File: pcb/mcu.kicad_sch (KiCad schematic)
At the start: 18 parts, among them J1 AVR-UPDI-6, U1 ATtiny1616-MNR

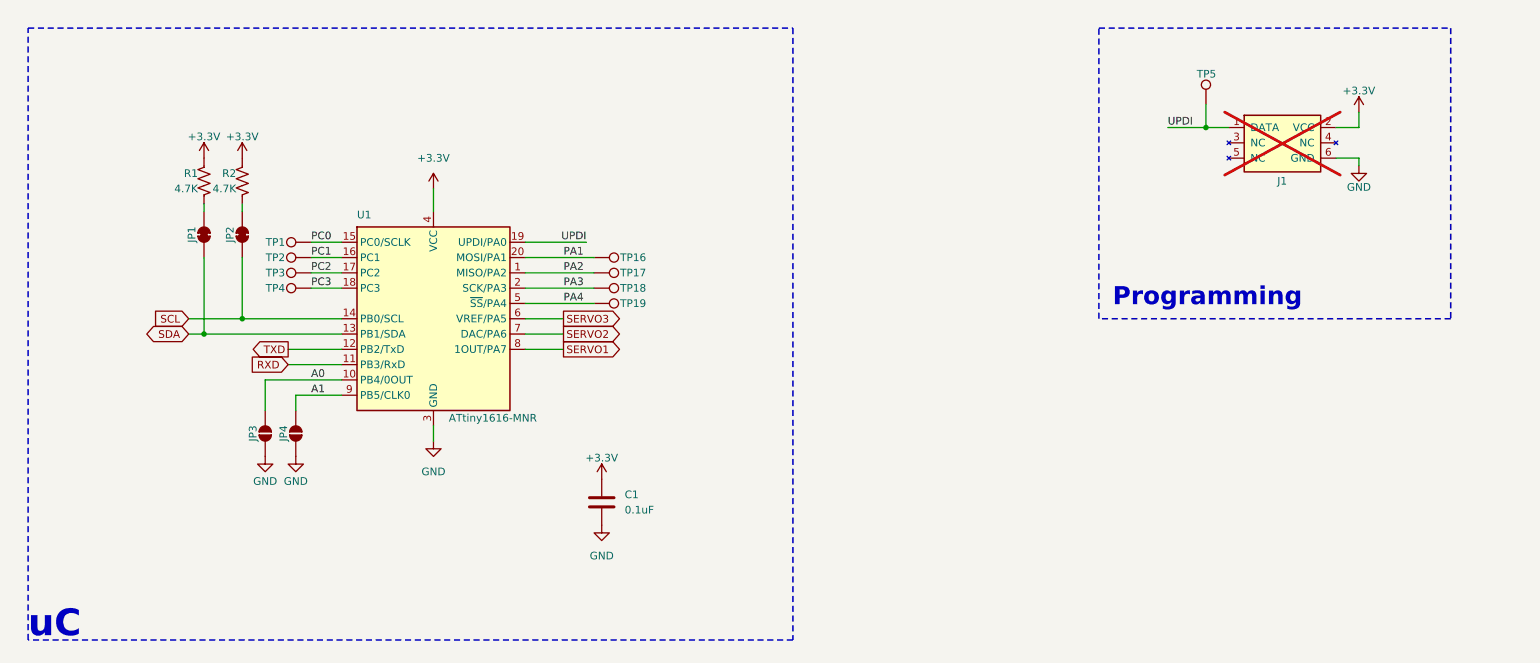
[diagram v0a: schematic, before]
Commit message: Added status leds
forced to reroute entire board
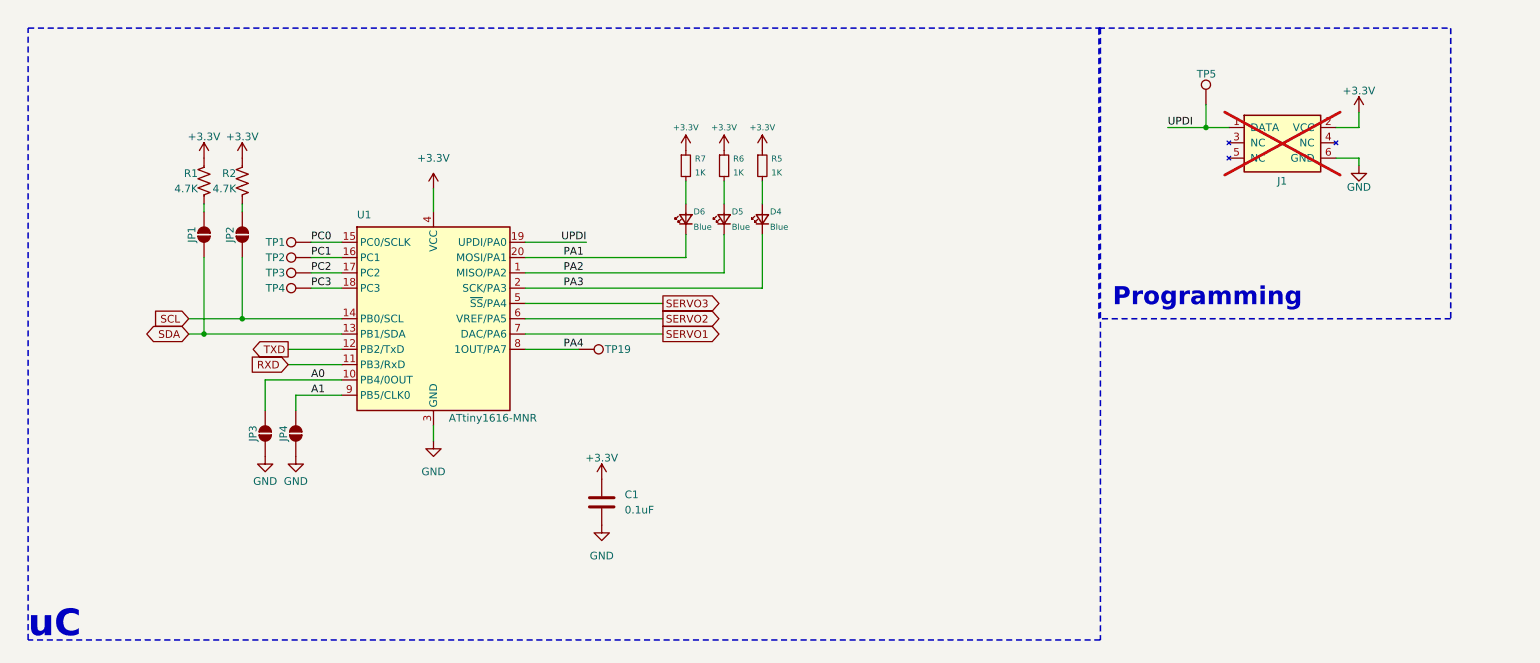
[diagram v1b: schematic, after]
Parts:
- removed TP16, TP17, TP18: ~, CRGM Mechanical:TestPoint_Pad_D1.0mm, symbol Connector:TestPoint
- added D4, D5, D6: Blue, CRGM Passive:LED_0603_1608Metric, symbol Device:LED_Small
- added R5, R6, R7: 1K, CRGM Passive:R_0603_1608Metric, symbol Device:R_Small
- JP1, JP2: footprint CRGM Connector:SolderJumper-2_P1.3mm_Bridged_RoundedPad1.0x1.5mm -> CRGM Connector:SolderJumper-2_P1.3mm_Open_RoundedPad1.0x1.5mm; symbol Jumper:SolderJumper_2_Bridged -> CRGM Connector:SolderJumper_2_Open
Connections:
- net +3.3V: now also R5.1, R6.1, R7.1
- net PA1: now also D6.1 (K)
- net PA2: now also D5.1 (K)
- net PA3: now also D4.1 (K)
- net PA4: now also U1.8 (1OUT/PA7); no longer U1.5 (~{SS}/PA4)
- net SERVO1: now also U1.7 (DAC/PA6); no longer U1.8 (1OUT/PA7)
- net SERVO2: now also U1.6 (VREF/PA5); no longer U1.7 (DAC/PA6)
- net SERVO3: now also U1.5 (~{SS}/PA4); no longer U1.6 (VREF/PA5)
- new net: D5.2 (A), R6.2
- new net: D6.2 (A), R7.2
- new net: D4.2 (A), R5.2
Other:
- moved on the sheet: TP19

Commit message: Added servo power and filtering
Added connection for servo power
Added solder jumper for servo power to 5V
Added caps to servo power
Added bulk decoupling caps
Added TVS to various inputs
Updated renders
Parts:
- removed C1: 0.1uF, CRGM Passive:C_0603_1608Metric, symbol Device:C
- added C1: 0.1uF, CRGM Passive:C_0603_1608Metric, symbol Device:C_Small
- renumbered D6 to D1, D5 to D2, D4 to D3, R7 to R3, R6 to R4, TP19 to TP5, TP5 to TP6
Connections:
- net +3.3V: now also C1.1
- net GND: now also C1.2

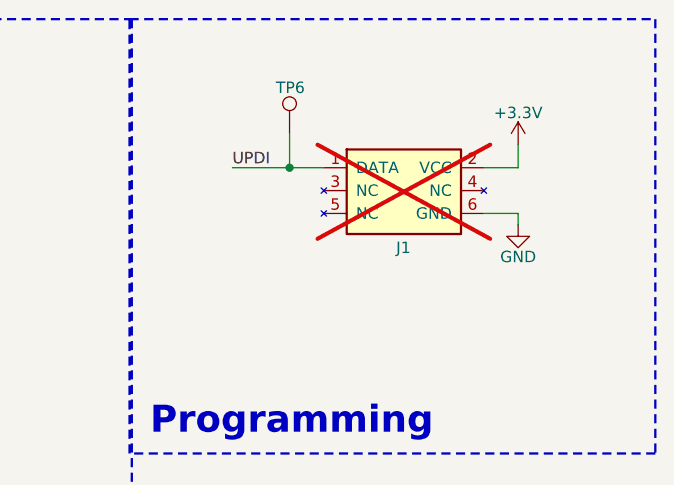
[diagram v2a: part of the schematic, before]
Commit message: Adjusting back on lessons learned from 1.1,
Added skilkscreen
Moved UART to UPDI connector
Created room for 4th servo connector?
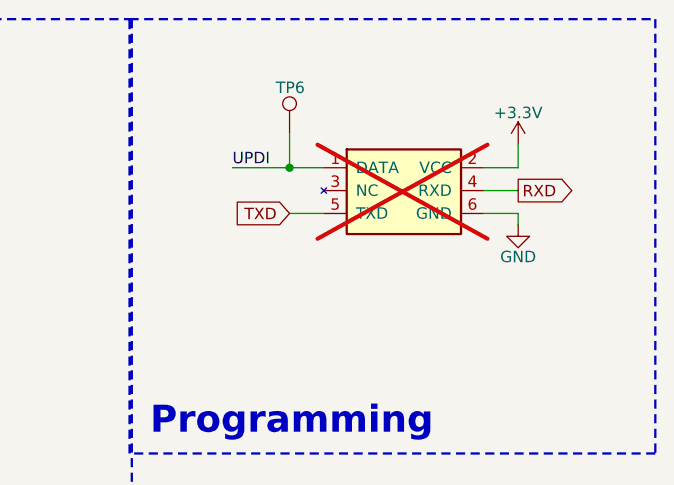
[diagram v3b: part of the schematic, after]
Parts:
- J1: symbol CRGM Connector:AVR-UPDI-6 -> CRGM Connector:AVR-UPDI-UART-6; now in the parts list
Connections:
- net RXD: now also J1.4 (RXD)
- net TXD: now also J1.5 (TXD)
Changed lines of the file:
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@@
+	(wire
+		(pts
+			(xy 246.38 44.45) (xy 242.57 44.45)
+		)
+		(stroke
+			(width 0)
+			(type default)
+		)
+	)
 	(wire
 		(pts
@@
 		(pts
 			(xy 107.95 78.74) (xy 116.84 78.74)
+		)
+		(stroke
+			(width 0)
+			(type default)
+		)
+	)
+	(wire
+		(pts
+			(xy 220.98 46.99) (xy 224.79 46.99)
 		)
 		(stroke
@@
 		(property "Intersheetrefs" "${INTERSHEET_REFS}"
 			(at 44.4054 76.2 0)
+			(effects
+				(font
+					(size 1.27 1.27)
+				)
+				(justify right)
+			)
+		)
+	)
+	(global_label "RXD"
+		(shape output)
+		(at 246.38 44.45 0)
+		(fields_autoplaced yes)
+		(effects
+			(font
+				(size 1.27 1.27)
+			)
+			(justify left)
+		)
+		(property "Intersheetrefs" "${INTERSHEET_REFS}"
+			(at 253.1147 44.45 0)
+			(effects
+				(font
+					(size 1.27 1.27)
+				)
+				(justify left)
+			)
+		)
+	)
+	(global_label "TXD"
+		(shape input)
+		(at 220.98 46.99 180)
+		(fields_autoplaced yes)
+		(effects
+			(font
+				(size 1.27 1.27)
+			)
+			(justify right)
+		)
+		(property "Intersheetrefs" "${INTERSHEET_REFS}"
+			(at 214.5477 46.99 0)
 			(effects
 				(font
@@
 	)
 	(symbol
-		(lib_id "CRGM Connector:AVR-UPDI-6")
+		(lib_id "CRGM Connector:AVR-UPDI-UART-6")
 		(at 233.68 45.72 0)
 		(unit 1)
 		(exclude_from_sim no)
-		(in_bom no)
+		(in_bom yes)
 		(on_board yes)
 		(dnp yes)
@@
 				)
 				(justify right)
+				(hide yes)
 			)
 		)
@@
 		)
 		(property "Footprint" "CRGM Connector:PinHeader_2x03_P2.54mm_Vertical_SMD"
-			(at 227.33 46.99 90)
+			(at 233.68 58.674 0)
 			(effects
 				(font
@@
 			)
 		)
-		(property "Description" "Atmel 6-pin UPDI connector"
+		(property "Description" "Atmel 6-pin UPDI + UART connector"
 			(at 233.68 56.388 0)
 			(effects

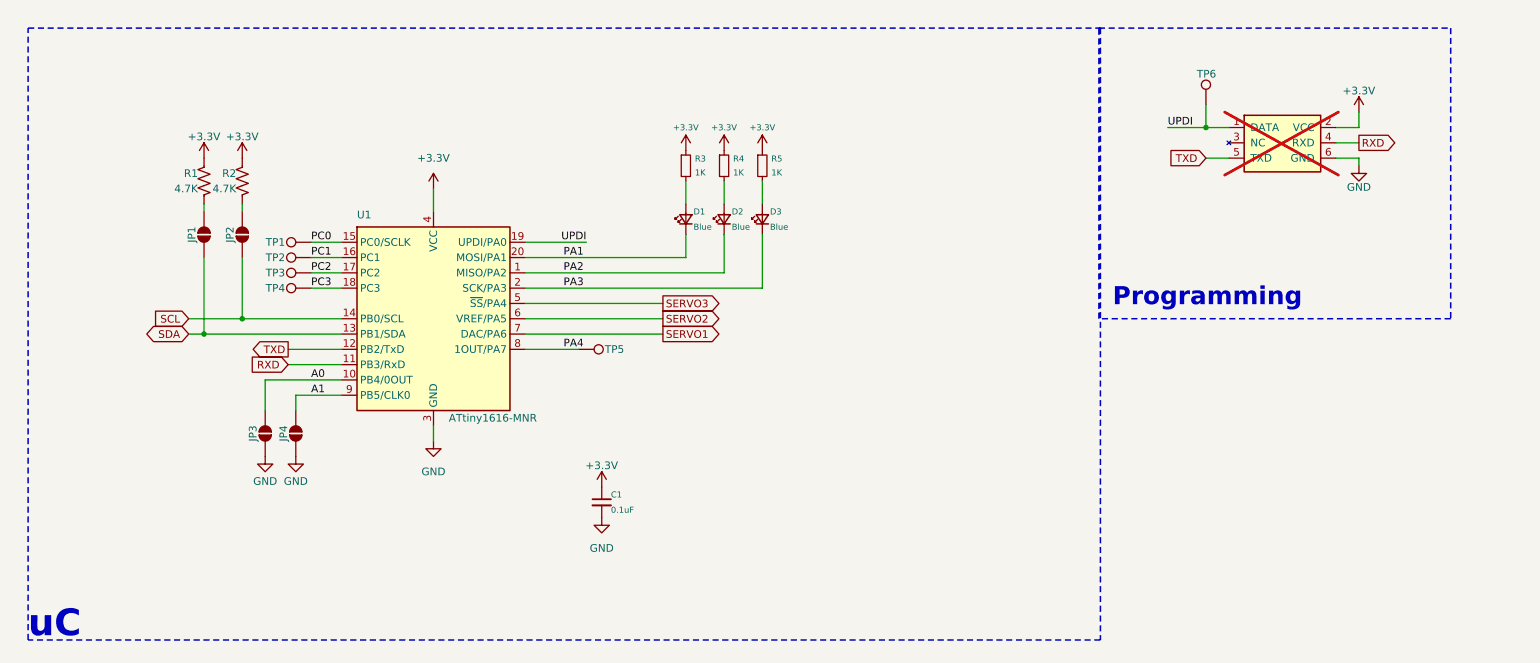
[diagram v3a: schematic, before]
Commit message: changed connectors to vertical
Updated connectors with ground on mounting points
Updated and rerouted
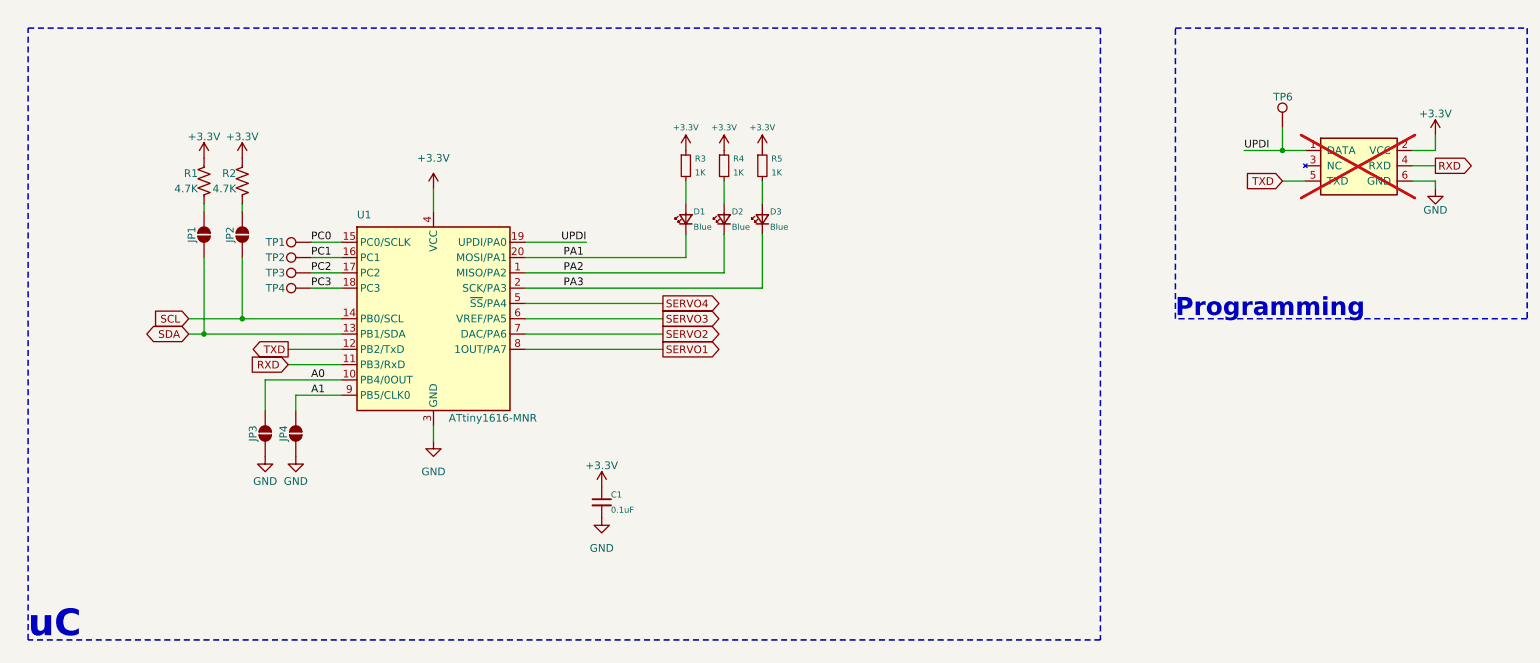
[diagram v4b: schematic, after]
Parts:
- removed TP5: ~, CRGM Mechanical:TestPoint_Pad_D1.0mm, symbol Connector:TestPoint
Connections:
- net PA4 is gone; now on net SERVO1: U1.8 (1OUT/PA7)
- net SERVO1: no longer U1.7 (DAC/PA6)
- net SERVO2: now also U1.7 (DAC/PA6); no longer U1.6 (VREF/PA5)
- net SERVO3: now also U1.6 (VREF/PA5); no longer U1.5 (~{SS}/PA4)
- new net SERVO4: U1.5 (~{SS}/PA4)
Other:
- moved on the sheet: TP6

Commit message: Finished routing
Updated renders
Added 4th LED
Fixed LED wiring
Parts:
- removed TP4: ~, CRGM Mechanical:TestPoint_Pad_D1.0mm, symbol Connector:TestPoint
- added D14: Blue, CRGM Passive:LED_0603_1608Metric, symbol Device:LED_Small
- added R9: 1K, CRGM Passive:R_0603_1608Metric, symbol Device:R_Small
- added TP4, TP5: ~, CRGM Mechanical:TestPoint_Pad_D1.0mm, symbol CRGM Connector:TestPoint
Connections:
- net +3.3V: now also R9.1
- net RXD: now also TP5.1
- net TXD: now also TP4.1
- net PA1 renamed SERVO3_LED
- net PA2 renamed SERVO2_LED
- net PA3 renamed SERVO1_LED
- net PC3 renamed SERVO4_LED
- net SERVO4_LED: now also D14.1 (K)
- new net: D14.2 (A), R9.2
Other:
- moved on the sheet: C1, D1, D2, D3, JP1, JP2, JP3, JP4, R1, R2, R3, R4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

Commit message: Removed space in MN for resistors
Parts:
- R1, R2: MN FOJAN -> FOJAN
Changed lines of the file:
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@@
 			)
 		)
-		(property "MN" "FOJAN "
+		(property "MN" "FOJAN"
 			(at 49.53 50.8 0)
 			(effects
@@
 			)
 		)
-		(property "MN" "FOJAN "
+		(property "MN" "FOJAN"
 			(at 55.88 50.8 0)
 			(effects

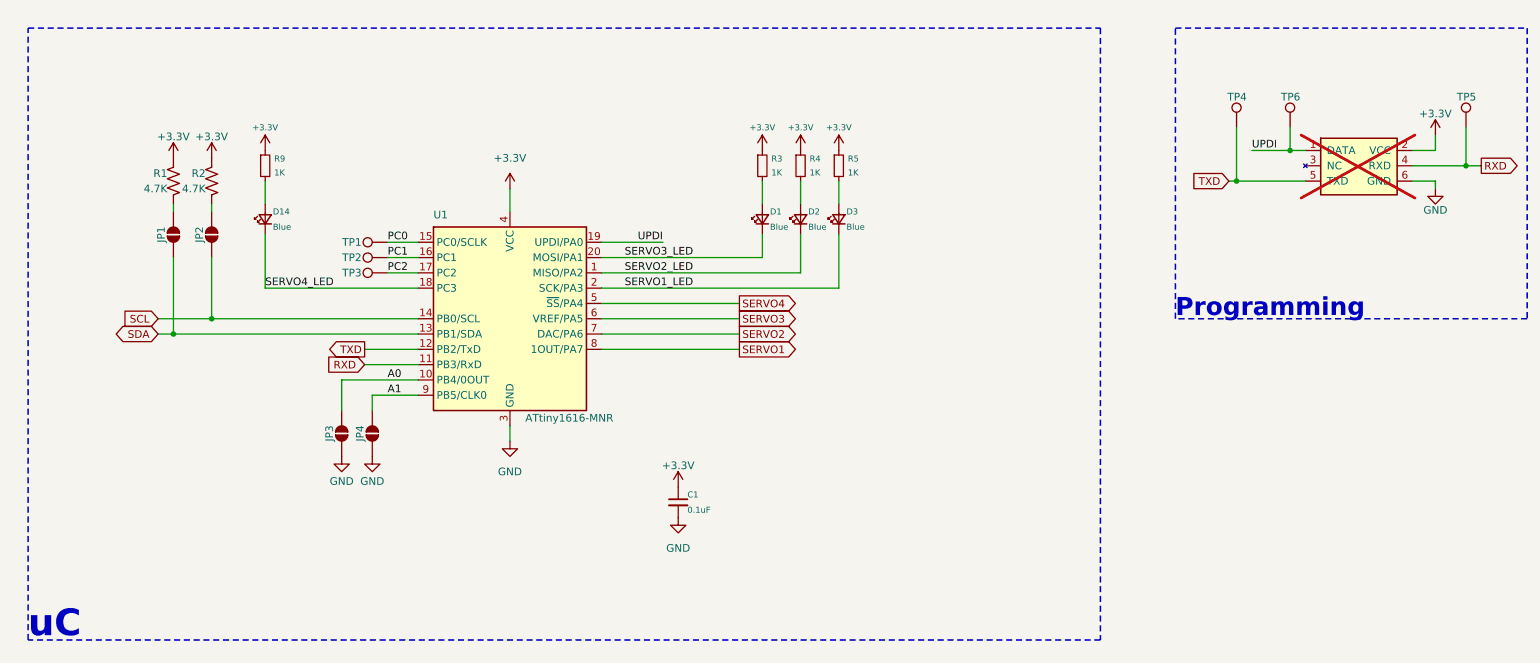
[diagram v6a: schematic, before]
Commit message: Redesign with SMT32
Complete redesign using SMT32 instead of ATTINY.
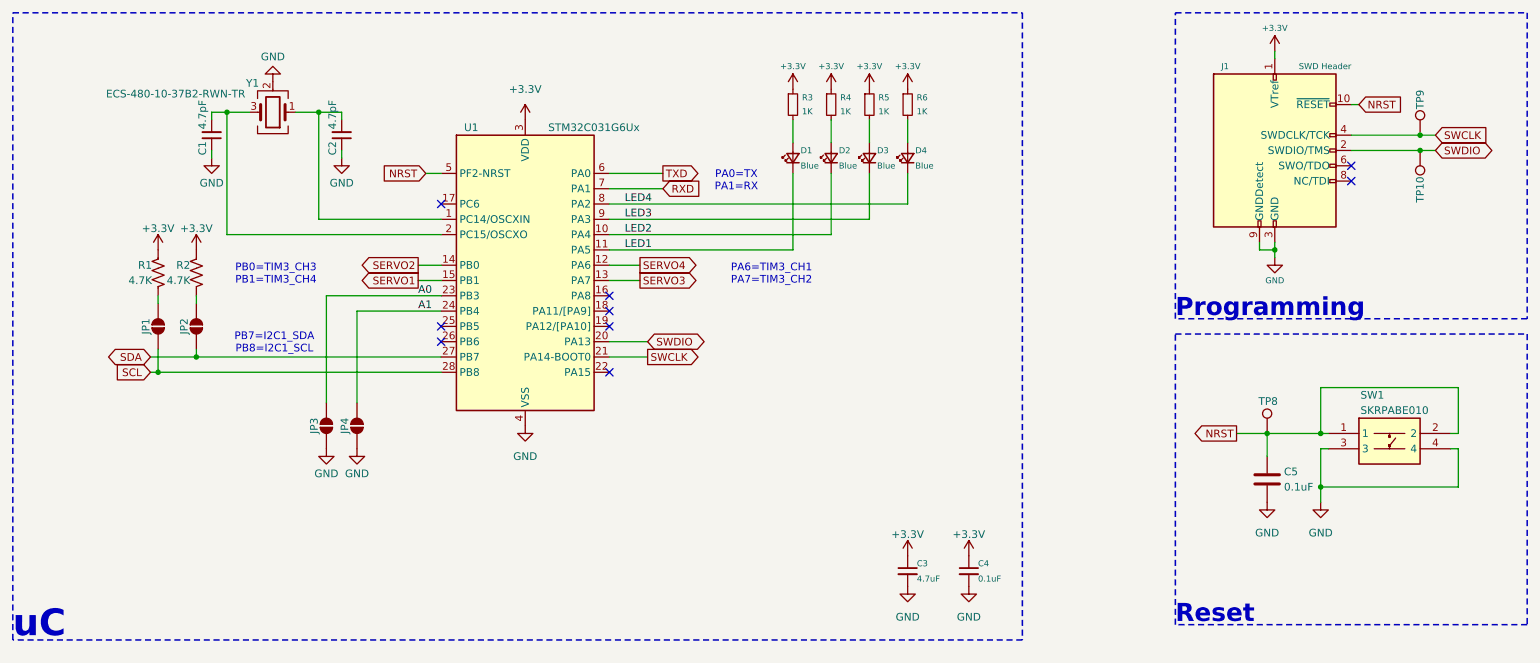
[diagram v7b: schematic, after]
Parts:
- removed J1: AVR-UPDI-6, CRGM Connector:PinHeader_2x03_P2.54mm_Vertical_SMD, symbol CRGM Connector:AVR-UPDI-UART-6
- removed TP1, TP2, TP3: ~, CRGM Mechanical:TestPoint_Pad_D1.0mm, symbol Connector:TestPoint
- removed TP4, TP5, TP6: ~, CRGM Mechanical:TestPoint_Pad_D1.0mm, symbol CRGM Connector:TestPoint
- removed U1: ATtiny1616-MNR, CRG Makes:VQFN-20-1EP_3x3mm_P0.4mm_EP1.7x1.7mm_ThermalVias, symbol CRG Makes:ATtiny1616-MNR
- added C1, C2: 4.7pF, CRGM Passive:C_0603_1608Metric, symbol CRGM Passive:C_Small
- added C3: 4.7uF, CRGM Passive:C_0603_1608Metric, symbol Device:C_Small
- added C5: 0.1uF, CRGM Passive:C_0603_1608Metric, symbol Device:C
- added J1: SWD Header, CRGM Connector:PinHeader_2x05_P1.27mm_Vertical_SMD, symbol Connector:Conn_ARM_JTAG_SWD_10
- added SW1: SKRPABE010, CRGM Switches:SMD-4P-4.2x3.2mm, symbol CRGM Switches:SKRPABE010
- added TP10, TP8, TP9: ~, CRGM Mechanical:TestPoint_Pad_D1.0mm, symbol Connector:TestPoint
- added U1: STM32C031G6Ux, CRG Makes:QFN-28_4x4mm_P0.5mm, symbol CRG Makes:STM32C031G6Ux
- added Y1: ECS-480-10-37B2-RWN-TR, CRGM Passive:Crystal_SMD_2016-4Pin_2.0x1.6mm, symbol CRGM Passive:ECS-480-10-37B2-RWN-TR
- R1, R2: MN FOJAN -> FOJAN
- renumbered C1 to C4, D14 to D4, R9 to R6
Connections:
- net +3.3V: now also C3.1, J1.1 (VTref), U1.3 (VDD)
- net A0: now also U1.23 (PB3)
- net A1: now also U1.24 (PB4)
- net GND: now also C1.1, C2.1, C3.2, C5.2, J1.3 (GND), J1.5 (GND), J1.9 (GNDDetect), SW1.3, SW1.4, U1.4 (VSS), Y1.2 (G), Y1.4 (G)
- net RXD: now also U1.7 (PA1)
- net SCL: now also JP1.1 (A), U1.28 (PB8); no longer JP2.1 (A)
- net SDA: now also JP2.1 (A), U1.27 (PB7); no longer JP1.1 (A)
- net SERVO1: now also U1.15 (PB1)
- net SERVO2: now also U1.14 (PB0)
- net SERVO3: now also U1.13 (PA7)
- net SERVO4: now also U1.12 (PA6)
- net TXD: now also U1.6 (PA0)
- net SERVO1_LED renamed LED3
- net LED3: now also U1.9 (PA3)
- net SERVO2_LED renamed LED2
- net LED2: now also U1.10 (PA4)
- net SERVO3_LED renamed LED1
- net LED1: now also U1.11 (PA5)
- net SERVO4_LED renamed LED4
- net LED4: now also U1.8 (PA2)
- new net: C2.2, U1.1 (PC14/OSCXIN), Y1.1
- new net: C1.2, U1.2 (PC15/OSCXO), Y1.3
- new net NRST: C5.1, J1.10 (~{RESET}), SW1.1, SW1.2, TP8.1, U1.5 (PF2-NRST)
- new net SWCLK: J1.4 (SWDCLK/TCK), TP9.1, U1.21 (PA14-BOOT0)
- new net SWDIO: J1.2 (SWDIO/TMS), TP10.1, U1.20 (PA13)
- no-connect marks 0 -> 9
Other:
- note added: "PA0=TX PA1=RX"
- note added: "PA6=TIM3_CH1 PA7=TIM3_CH2"
- note added: "PB0=TIM3_CH3 PB1=TIM3_CH4"
- note added: "PB7=I2C1_SDA PB8=I2C1_SCL"
- note added: "Reset"
- moved on the sheet: C4, D1, D2, D3, D4, JP1, JP2, JP3, JP4, R1, R2, R3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

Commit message: Fixed models; adjusted layout
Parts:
- removed TP8: ~, CRGM Mechanical:TestPoint_Pad_D1.0mm, symbol Connector:TestPoint
- added TP1, TP2, TP3: ~, CRGM Mechanical:TestPoint_Pad_D1.0mm, symbol Connector:TestPoint
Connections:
- net +3.3V: now also TP2.1
- net GND: now also TP3.1
- net NRST: now also TP1.1
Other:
- moved on the sheet: J1, TP10, TP9
